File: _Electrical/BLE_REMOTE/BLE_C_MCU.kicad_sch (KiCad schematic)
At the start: 16 parts, among them J1 PGRM, J2 Conn_01x02_Pin, U1 nRF52832-QFxx, Y1 Crystal_GND24

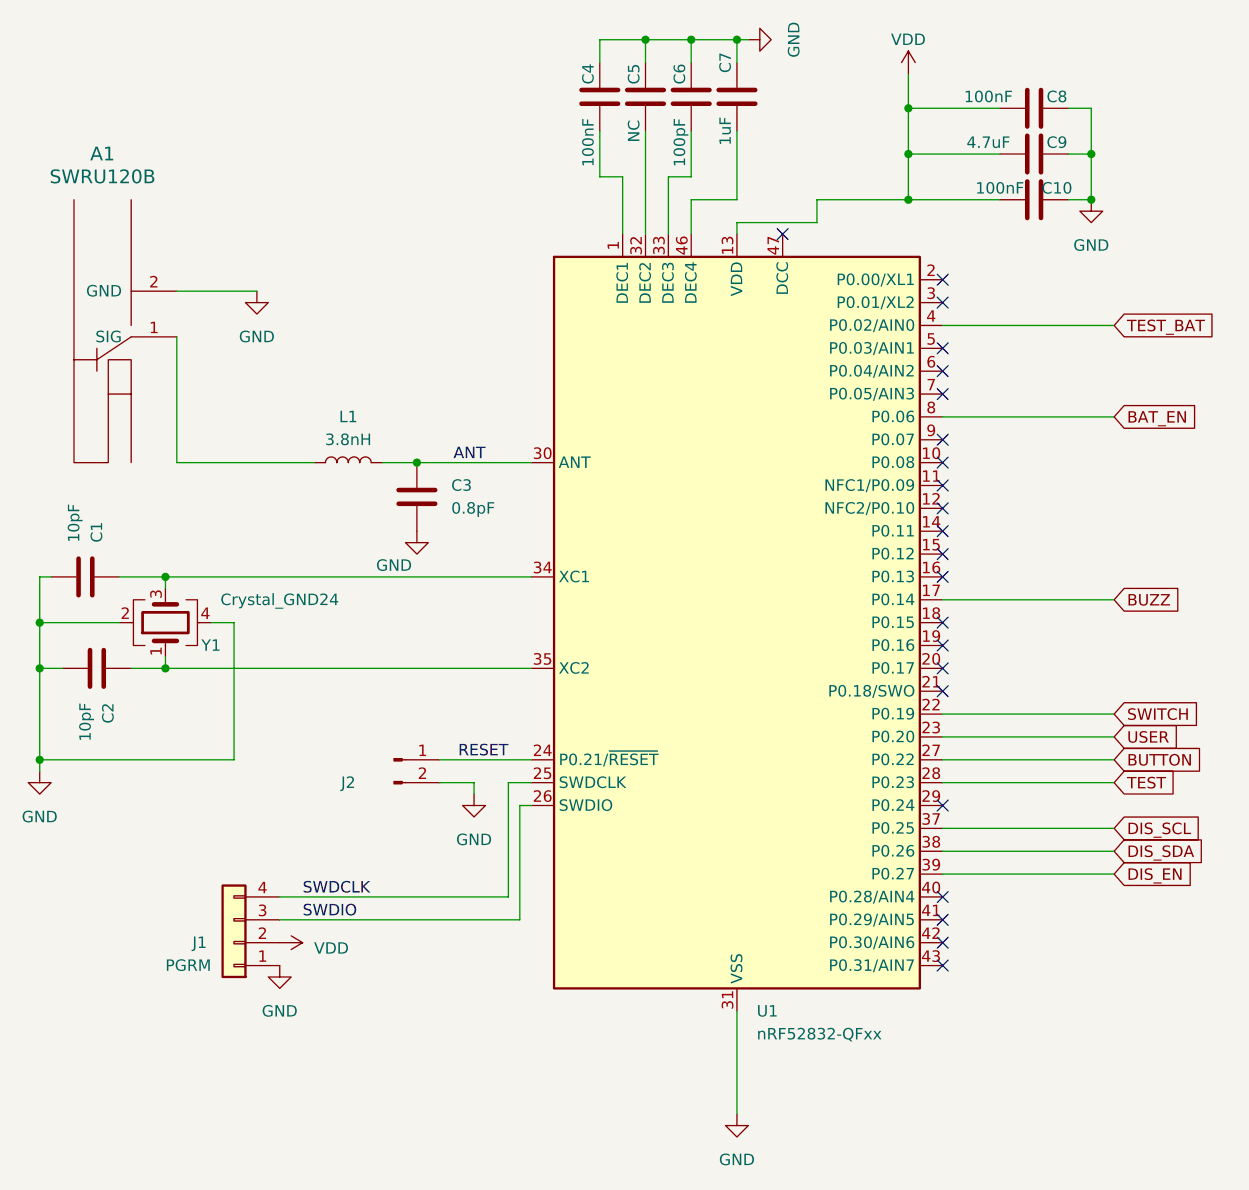
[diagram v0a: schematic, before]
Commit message: Added simulation and updated power button
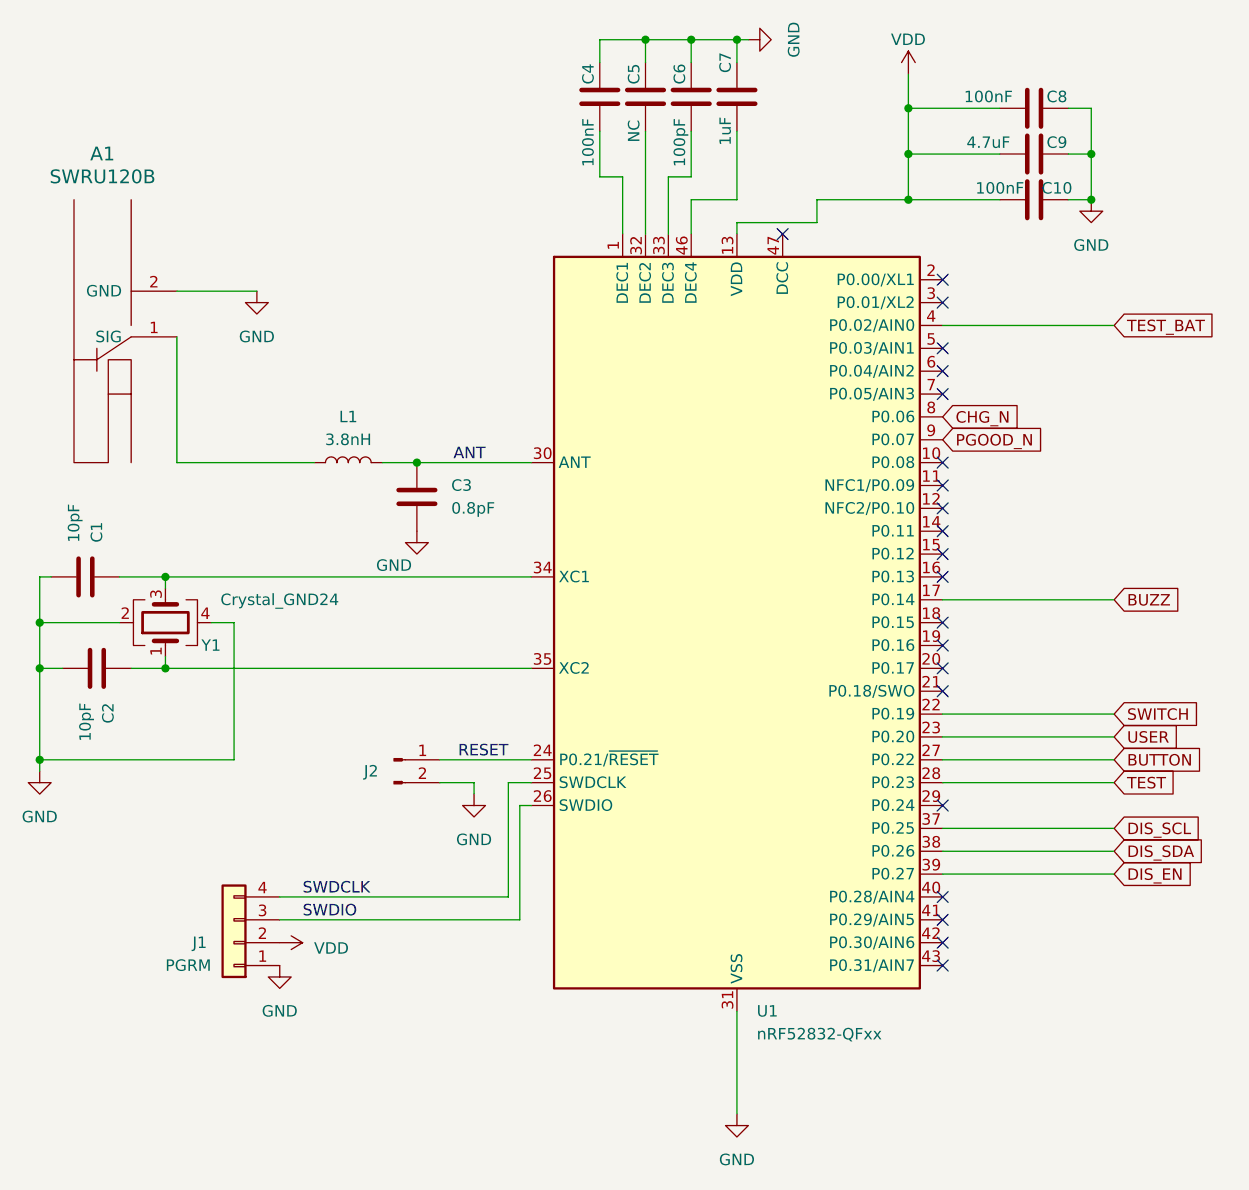
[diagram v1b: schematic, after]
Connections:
- net PGOOD_N: now reaches U1.9 (P0.07)
- net BAT_EN renamed CHG_N
- no-connect marks 22 -> 21
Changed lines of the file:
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@@
   (no_connect (at 137.16 107.95))
   (no_connect (at 137.16 140.97))
-  (no_connect (at 137.16 82.55))
   (no_connect (at 137.16 85.09))
   (no_connect (at 137.16 90.17))
@@
     (stroke (width 0) (type default))
   )
-  (wire (pts (xy 156.21 80.01) (xy 137.16 80.01))
-    (stroke (width 0) (type default))
-  )
   (wire (pts (xy 114.3 146.05) (xy 114.3 157.48))
     (stroke (width 0) (type default))
@@
     )
   )
+  (global_label "CHG_N" (shape input) (at 137.16 80.01 0) (fields_autoplaced)
+    (effects (font (size 1.27 1.27)) (justify left))
+    (property "Intersheetrefs" "${INTERSHEET_REFS}" (at 146.3138 80.01 0)
+      (effects (font (size 1.27 1.27)) (justify left) hide)
+    )
+  )
   (global_label "DIS_SDA" (shape input) (at 156.21 128.27 0) (fields_autoplaced)
     (effects (font (size 1.27 1.27)) (justify left))
@@
     )
   )
+  (global_label "PGOOD_N" (shape input) (at 137.16 82.55 0) (fields_autoplaced)
+    (effects (font (size 1.27 1.27)) (justify left))
+    (property "Intersheetrefs" "${INTERSHEET_REFS}" (at 148.9143 82.55 0)
+      (effects (font (size 1.27 1.27)) (justify left) hide)
+    )
+  )
   (global_label "SWITCH" (shape input) (at 156.21 113.03 0) (fields_autoplaced)
     (effects (font (size 1.27 1.27)) (justify left))
@@
     )
   )
-  (global_label "BAT_EN" (shape input) (at 156.21 80.01 0) (fields_autoplaced)
-    (effects (font (size 1.27 1.27)) (justify left))
-    (property "Intersheetrefs" "${INTERSHEET_REFS}" (at 165.9685 80.01 0)
-      (effects (font (size 1.27 1.27)) (justify left) hide)
-    )
-  )
   (global_label "BUZZ" (shape input) (at 156.21 100.33 0) (fields_autoplaced)
     (effects (font (size 1.27 1.27)) (justify left))
@@
     (effects (font (size 1.27 1.27)) (justify left bottom))
     (property "Netclass" "HF" (at 87.0585 105.41 0)
-      (effects (font (size 1.27 1.27) italic) (justify left))
-    )
-  )
-  (netclass_flag "" (length 2.54) (shape round) (at 140.97 80.01 0) (fields_autoplaced)
-    (effects (font (size 1.27 1.27)) (justify left bottom))
-    (property "Netclass" "Signal" (at 141.6685 77.47 0)
       (effects (font (size 1.27 1.27) italic) (justify left))
     )
@@
   (symbol (lib_id "Connector:Conn_01x02_Pin") (at 76.2 118.11 0) (unit 1)
     (in_bom yes) (on_board yes) (dnp no)
-    (property "Reference" "J2" (at 71.12 120.65 0)
-      (effects (font (size 1.27 1.27)))
-    )
+    (property "Reference" "J2" (at 73.66 119.38 0)
+      (effects (font (size 1.27 1.27)))
+    )

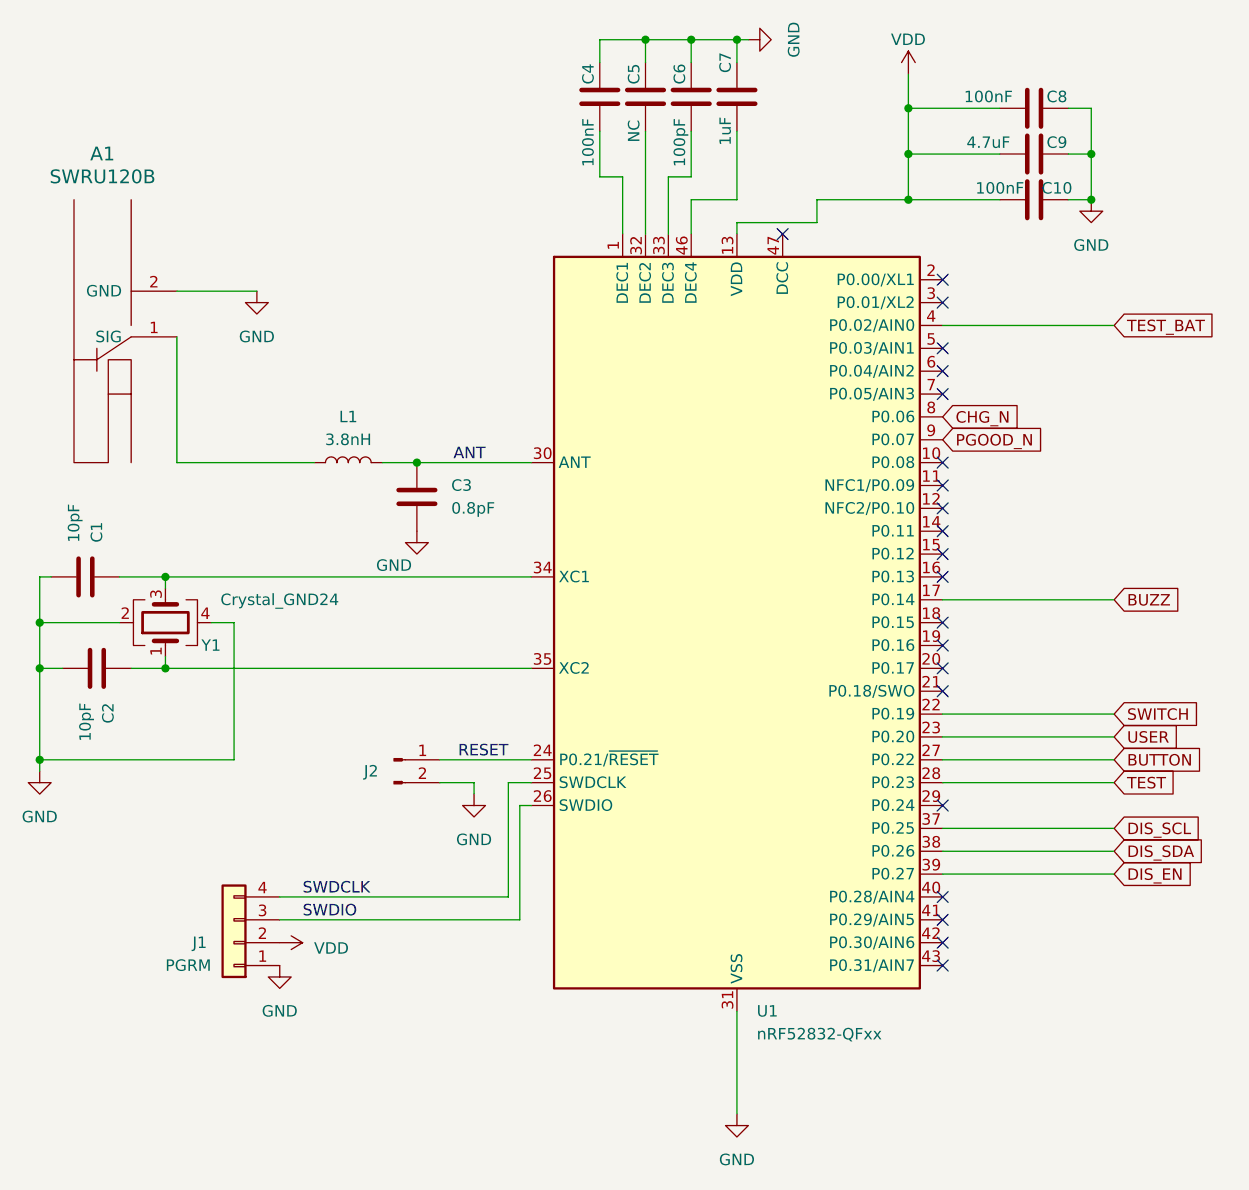
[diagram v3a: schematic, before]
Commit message: Finished initial PCB draft
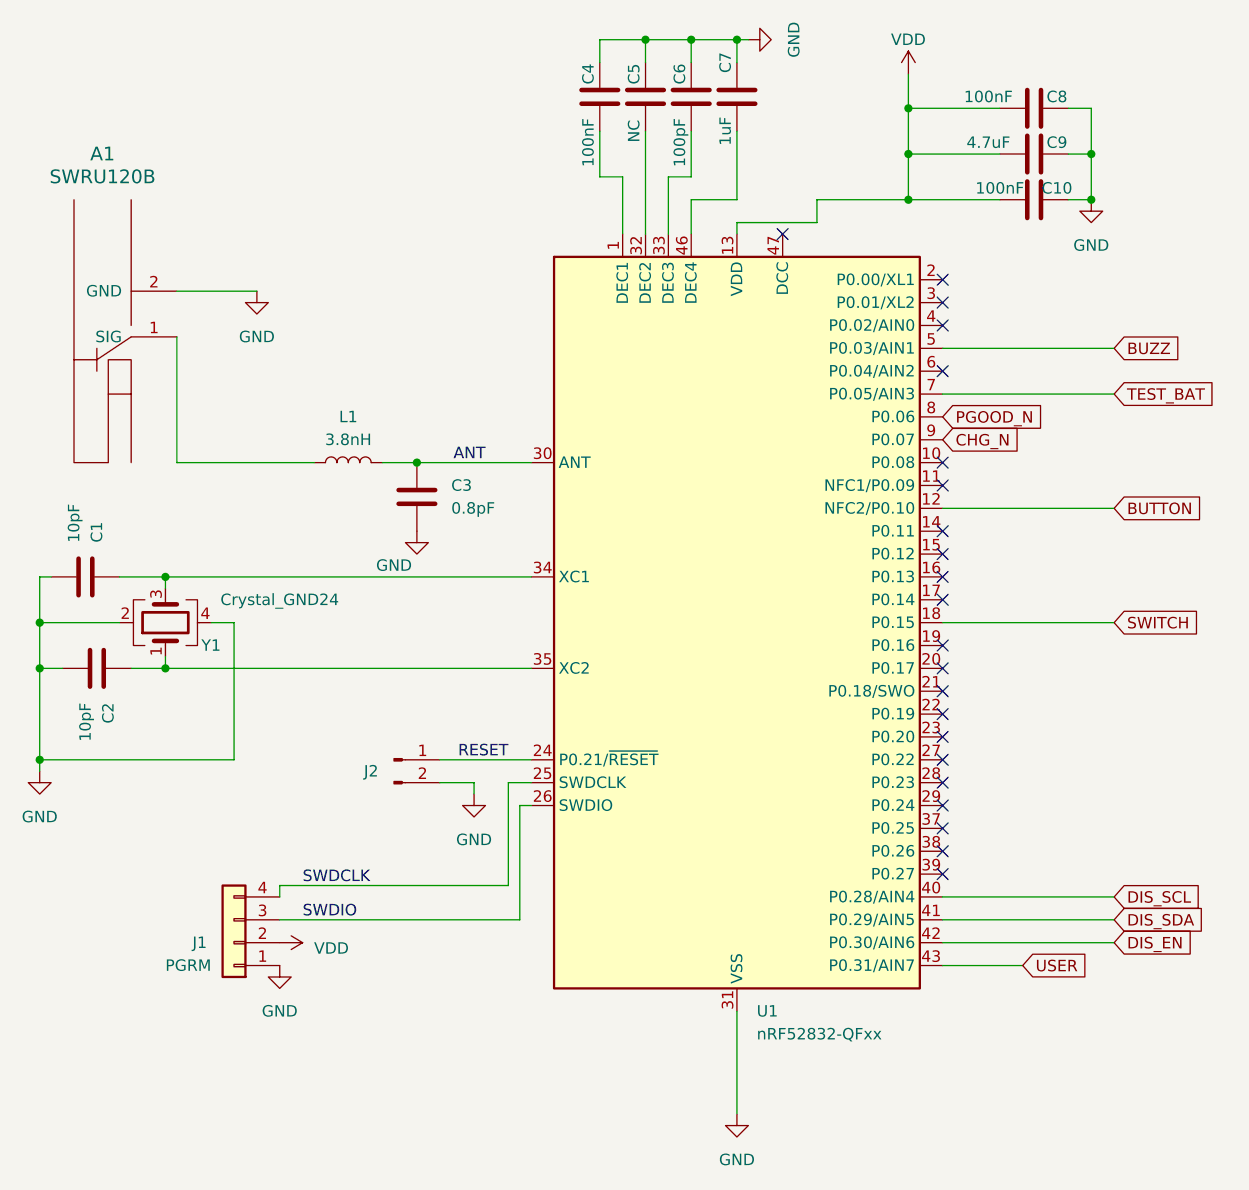
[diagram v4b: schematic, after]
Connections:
- net BUTTON: now also U1.12 (NFC2/P0.10); no longer U1.27 (P0.22)
- net BUZZ: now also U1.5 (P0.03/AIN1); no longer U1.17 (P0.14)
- net CHG_N: now also U1.9 (P0.07); no longer U1.8 (P0.06)
- net DIS_EN: now also U1.42 (P0.30/AIN6); no longer U1.39 (P0.27)
- net DIS_SCL: now also U1.40 (P0.28/AIN4); no longer U1.37 (P0.25)
- net DIS_SDA: now also U1.41 (P0.29/AIN5); no longer U1.38 (P0.26)
- net PGOOD_N: now also U1.8 (P0.06); no longer U1.9 (P0.07)
- net SWITCH: now also U1.18 (P0.15); no longer U1.22 (P0.19)
- net TEST_BAT: now also U1.7 (P0.05/AIN3); no longer U1.4 (P0.02/AIN0)
- net USER: now also U1.43 (P0.31/AIN7); no longer U1.23 (P0.20)
- net TEST: no longer names the net of U1.28 (P0.23)
- no-connect marks 21 -> 22

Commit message: finished initial PCB draft
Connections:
- net BUTTON: now also U1.15 (P0.12); no longer U1.12 (NFC2/P0.10)
- net GND: now also A1.4, A1.5
- net LED_D: now reaches U1.11 (NFC1/P0.09)
- no-connect marks 22 -> 20
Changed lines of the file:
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@@
   (junction (at 36.83 102.87) (diameter 0) (color 0 0 0 0)
+  )
+  (junction (at 54.61 66.04) (diameter 0) (color 0 0 0 0)
   )
   (junction (at 153.67 50.8) (diameter 0) (color 0 0 0 0)
@@
   (no_connect (at 119.38 59.69))
   (no_connect (at 137.16 123.19))
-  (no_connect (at 137.16 92.71))
+  (no_connect (at 137.16 90.17))
   (no_connect (at 137.16 67.31))
   (no_connect (at 137.16 97.79))
@@
   (no_connect (at 137.16 107.95))
   (no_connect (at 137.16 113.03))
-  (no_connect (at 137.16 87.63))
   (no_connect (at 137.16 130.81))
-  (no_connect (at 137.16 85.09))
+  (no_connect (at 137.16 92.71))
   (no_connect (at 137.16 100.33))
-  (no_connect (at 137.16 95.25))
   (no_connect (at 137.16 128.27))
   (no_connect (at 137.16 120.65))
@@
     (stroke (width 0) (type default))
   )
+  (wire (pts (xy 49.53 82.55) (xy 49.53 87.63))
+    (stroke (width 0) (type default))
+  )
   (wire (pts (xy 101.6 59.69) (xy 101.6 53.34))
     (stroke (width 0) (type default))
@@
     (stroke (width 0) (type default))
   )
+  (wire (pts (xy 54.61 66.04) (xy 60.96 66.04))
+    (stroke (width 0) (type default))
+  )
   (wire (pts (xy 88.9 132.08) (xy 88.9 120.65))
     (stroke (width 0) (type default))
@@
     (stroke (width 0) (type default))
   )
+  (wire (pts (xy 156.21 95.25) (xy 137.16 95.25))
+    (stroke (width 0) (type default))
+  )
   (wire (pts (xy 50.8 97.79) (xy 91.44 97.79))
     (stroke (width 0) (type default))
@@
     (stroke (width 0) (type default))
   )
+  (wire (pts (xy 49.53 59.69) (xy 54.61 59.69))
+    (stroke (width 0) (type default))
+  )
   (wire (pts (xy 36.83 97.79) (xy 38.1 97.79))
     (stroke (width 0) (type default))
@@
     (stroke (width 0) (type default))
   )
-  (wire (pts (xy 156.21 90.17) (xy 137.16 90.17))
+  (wire (pts (xy 54.61 59.69) (xy 54.61 66.04))
     (stroke (width 0) (type default))
   )
@@
     (stroke (width 0) (type default))
   )
-  (wire (pts (xy 52.07 66.04) (xy 60.96 66.04))
+  (wire (pts (xy 52.07 66.04) (xy 54.61 66.04))
     (stroke (width 0) (type default))
   )
@@
     )
   )
+  (global_label "BUTTON" (shape input) (at 156.21 95.25 0) (fields_autoplaced)
+    (effects (font (size 1.27 1.27)) (justify left))
+    (property "Intersheetrefs" "${INTERSHEET_REFS}" (at 166.3125 95.25 0)
+      (effects (font (size 1.27 1.27)) (justify left) hide)
+    )
+  )
   (global_label "PGOOD_N" (shape input) (at 137.16 80.01 0) (fields_autoplaced)
     (effects (font (size 1.27 1.27)) (justify left))
@@
     )
   )
+  (global_label "LED_D" (shape input) (at 137.16 87.63 0) (fields_autoplaced)
+    (effects (font (size 1.27 1.27)) (justify left))
+    (property "Intersheetrefs" "${INTERSHEET_REFS}" (at 145.7505 87.63 0)
+      (effects (font (size 1.27 1.27)) (justify left) hide)
+    )
+  )
   (global_label "DIS_SCL" (shape input) (at 156.21 133.35 0) (fields_autoplaced)
     (effects (font (size 1.27 1.27)) (justify left))
     (property "Intersheetrefs" "${INTERSHEET_REFS}" (at 166.6753 133.35 0)
-      (effects (font (size 1.27 1.27)) (justify left) hide)
-    )
-  )
-  (global_label "BUTTON" (shape input) (at 156.21 90.17 0) (fields_autoplaced)
-    (effects (font (size 1.27 1.27)) (justify left))
-    (property "Intersheetrefs" "${INTERSHEET_REFS}" (at 166.3125 90.17 0)
       (effects (font (size 1.27 1.27)) (justify left) hide)
     )
@@
     )
   )
-  (netclass_flag "" (length 2.54) (shape round) (at 146.05 90.17 0) (fields_autoplaced)
-    (effects (font (size 1.27 1.27)) (justify left bottom))
-    (property "Netclass" "Signal" (at 146.7485 87.63 0)
-      (effects (font (size 1.27 1.27) italic) (justify left))
-    )
-  )
   (netclass_flag "" (length 2.54) (shape round) (at 57.15 85.09 0) (fields_autoplaced)
     (effects (font (size 1.27 1.27)) (justify left bottom))
@@
     (effects (font (size 1.27 1.27)) (justify left bottom))
     (property "Netclass" "HF" (at 87.0585 95.25 0)
+      (effects (font (size 1.27 1.27) italic) (justify left))
+    )
+  )
+  (netclass_flag "" (length 2.54) (shape round) (at 146.05 95.25 0) (fields_autoplaced)
+    (effects (font (size 1.27 1.27)) (justify left bottom))
+    (property "Netclass" "Signal" (at 146.7485 92.71 0)
       (effects (font (size 1.27 1.27) italic) (justify left))
     )
@@
         (path "/3c7105d6-b2e1-4841-966d-0562ae88783f/3c7d46da-db2c-458d-86d8-33d657630bb5"
           (reference "C9") (unit 1)
+        )
+      )
+    )
+  )
+  (symbol (lib_id "power:GND") (at 49.53 87.63 0) (unit 1)
+    (in_bom yes) (on_board yes) (dnp no) (fields_autoplaced)
+    (property "Reference" "#PWR041" (at 49.53 93.98 0)
+      (effects (font (size 1.27 1.27)) hide)
+    )
+    (property "Value" "GND" (at 49.53 92.71 0)
+      (effects (font (size 1.27 1.27)))
+    )
+    (property "Footprint" "" (at 49.53 87.63 0)
+      (effects (font (size 1.27 1.27)) hide)
+    )
+    (property "Datasheet" "" (at 49.53 87.63 0)
+      (effects (font (size 1.27 1.27)) hide)
+    )
+    (pin "1")
+    (instances
+      (project "BLE_REMOTE"
+        (path "/3c7105d6-b2e1-4841-966d-0562ae88783f/3c7d46da-db2c-458d-86d8-33d657630bb5"
+          (reference "#PWR041") (unit 1)
         )
       )
@@
       (effects (font (size 1.524 1.524)) hide)
     )
+    (pin "4")
+    (pin "5")
     (pin "1")
     (pin "2")
